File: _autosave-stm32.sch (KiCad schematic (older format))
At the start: 43 parts, among them J1 USB_B_Micro, J2 Conn_02x05_Odd_Even, J3 Conn_01x02, SW1 SW_Push, SW2 SW_Push, U1 STM32F407VGT6, U5 LM1117-3.3, X1 8MHz 20pF, Y2 32768 Hz

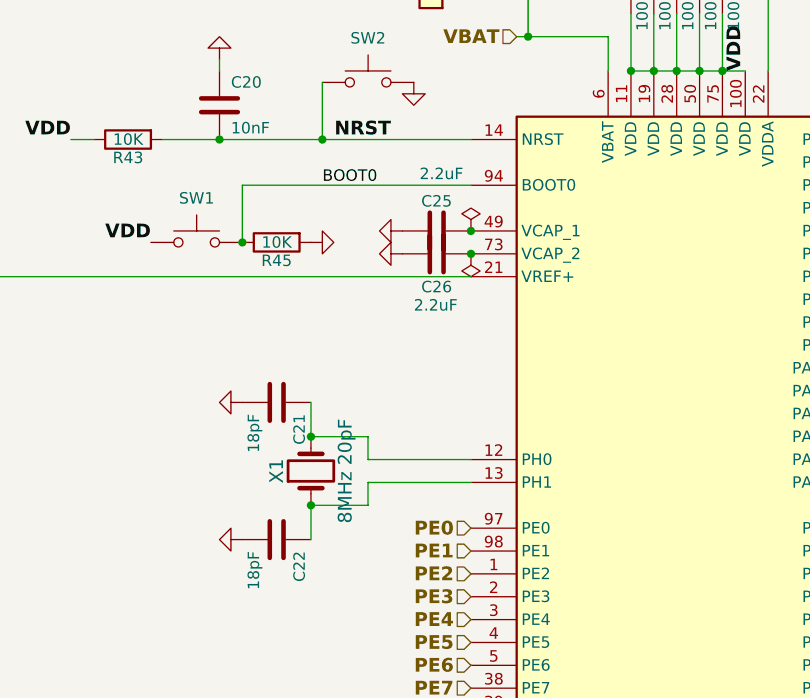
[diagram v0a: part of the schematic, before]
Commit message: Re-worked layout, wider traces, segregated ground current, opened area (#110)
* Add files via upload

* cover bolt info from stefanst

* Re-organized top vs bottom components.  Fixed footprint

* Moved GP5/6 voltage selection to center.

* Significant revision of schematic and layout:

Added reverse voltage protection.
Split 12V supply into a 12V-Key (ignition) pin and a 12V-MRel (supply from
main relay) pin.  The 12V main relay is controlled by the MRel pin to protect against reverse voltage and over-voltage.

The board can optionally draw under 1mA from the main relay coil to power
standby features, including CAN monitoring.

Increased the size of several resistors, notably ignition output resistors
and CAN termination, to handle typical power draw.

Changed resistor dividers to individual resistors for better accuracy than
typical resistor networks.

Standardized pull-up and pull-down resistors to 10K.

Changed to a tab-output regulator.

* Includes all known errata, except for component rotation for JLCPCB fabrication.

Includes
  Refined reverse protection layout with dual SS54 diodes
  Load dump protection, SMB TVS for 33V TVS
  Multiple footprints for Flash (SO-16, SO-8-208 and SO-8-150)
  Simplified pull-up and pull-down resistors, omitting unneeded ones
  Individual resistors for resistor dividers for easier sourcing of
    1% precision (most resistor networks are 5%, most 0603 parts are 1%).
  PicoBlade connector for RTC battery, matches low-cost laptop 2032 cells
  Clamping diode arrays on top, alternate BAS70 on bottom
  Options for VR input modification, and analog pull-ups on bottom.
  LM1117 voltage regulator footprint

* Added 2x5 header for SPI/serial communications
Connected LIN to PD8/PD9 USART3, output on SMD testpoint.
Added standby regulator.
Changed footprints of reverse protection diodes to SMA.
Rotated two opamps and clamping diode arrays for cleaner layout.
Moved status LEDs over for better silk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
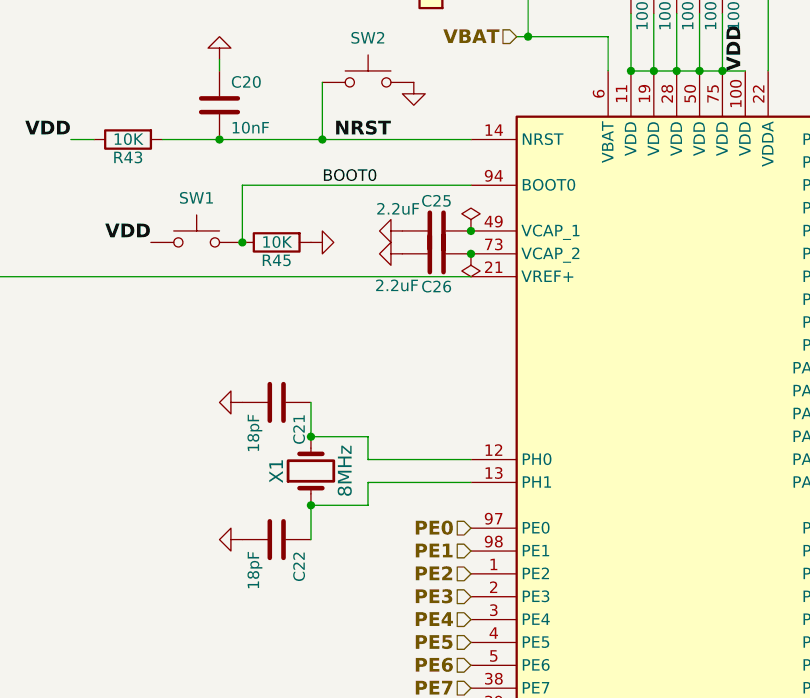
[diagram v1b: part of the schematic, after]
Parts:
- X1: value 8MHz 20pF -> 8MHz
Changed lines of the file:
@@
 Sheet 5 7
 Title "microRusEfi-2L"
-Date "2019-10-08"
+Date "2019-10-06"
 Rev "R0.4.5"
 Comp "rusEFI.com"
@@
 P 5400 4250
 F 0 "C25" V 5270 4250 50  0000 C CNN
-F 1 "2.2uF" V 5150 4175 50  0000 L CNN
+F 1 "2.2uF" V 5305 3985 50  0000 L CNN
 F 2 "Capacitor_SMD:C_0603_1608Metric" V -670 -850 60  0001 C CNN
 F 3 "" H 5400 4250 60  0001 C CNN
@@
 P 5400 4350
 F 0 "C26" V 5545 4350 50  0000 C CNN
-F 1 "2.2uF" V 5625 4250 50  0000 L CNN
+F 1 "2.2uF" V 5540 4080 50  0000 L CNN
 F 2 "Capacitor_SMD:C_0603_1608Metric" V -1170 -750 60  0001 C CNN
 F 3 "" H 5400 4350 60  0001 C CNN
@@
 $EndComp
 Connection ~ 4850 5150
+$Comp
+L Device:Crystal X1
+U 1 1 52D13AFB
+P 4850 5300
+F 0 "X1" H 4850 5450 60  0000 C CNN
+F 1 "8MHz" H 4850 5150 60  0000 C CNN
+F 2 "Crystal:Crystal_SMD_5032-2Pin_5.0x3.2mm" H 4850 5300 60  0001 C CNN
+F 3 "" H 4850 5300 60  0001 C CNN
+F 4 "stm32f407_board" H 16200 4825 60  0001 C CNN "PageName"
+F 5 "C115962" H 4850 5300 50  0001 C CNN "LCSC"
+	1    4850 5300
+	0    -1   -1   0
+$EndComp
 Wire Wire Line
 	5100 5350 5100 5450
@@
 Wire Wire Line
 	5575 3225 5800 3225
-$Comp
-L Device:Crystal X1
-U 1 1 52D13AFB
-P 4850 5300
-F 0 "X1" H 4850 5450 60  0000 C CNN
-F 1 "8MHz 20pF" H 4850 5150 60  0000 C CNN
-F 2 "Crystal:Crystal_SMD_5032-2Pin_5.0x3.2mm" H 4850 5300 60  0001 C CNN
-F 3 "" H 4850 5300 60  0001 C CNN
-F 4 "stm32f407_board" H 16200 4825 60  0001 C CNN "PageName"
-F 5 "C115962" H 4850 5300 50  0001 C CNN "LCSC"
-	1    4850 5300
-	0    -1   -1   0
-$EndComp
 $EndSCHEMATC
